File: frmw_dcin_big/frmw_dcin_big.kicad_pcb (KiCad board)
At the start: 2 copper layers, 41.5 x 24 mm, 55 parts, among them J2 SMART, M1 AltmodeFriend, Q1 SI4909, Q2 2N7002, Q3 2N7002, Q4 2N7002, Q5 SI4909, Q6 2N7002, Q7 SI4909, U1 SY6280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

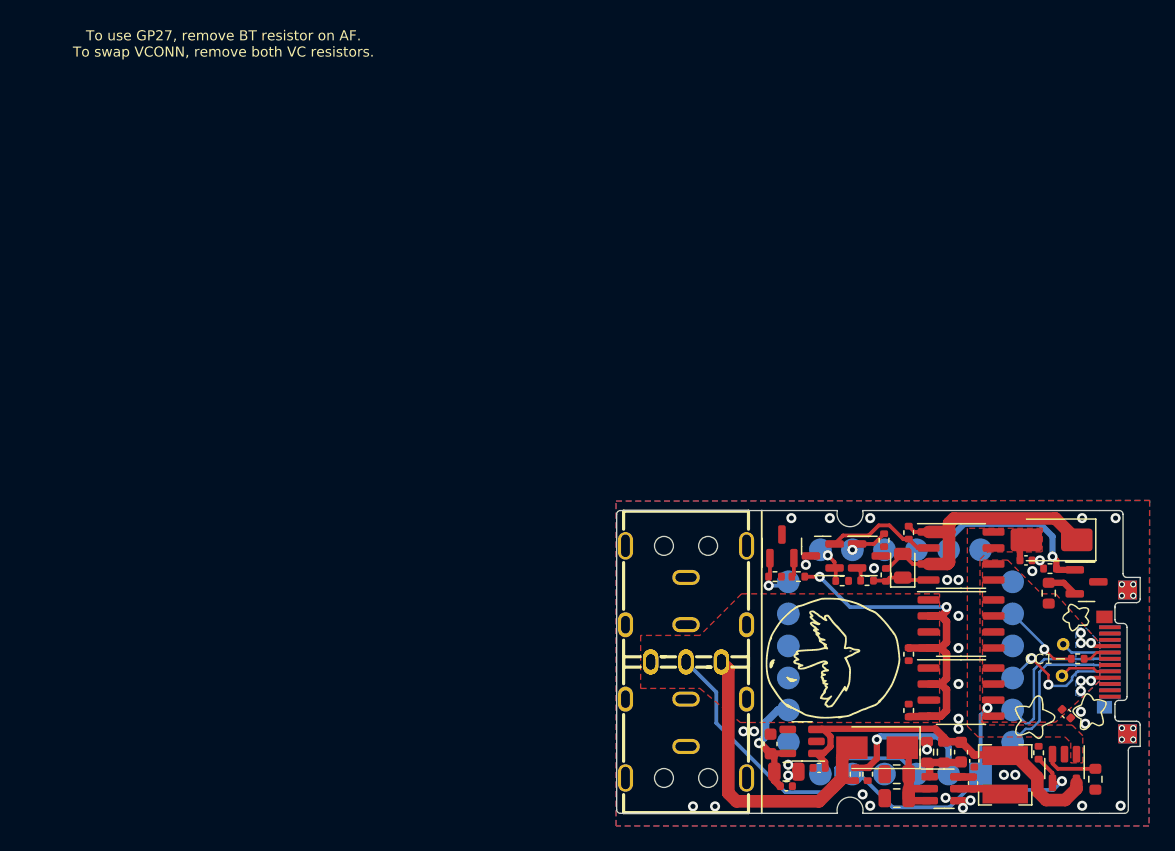
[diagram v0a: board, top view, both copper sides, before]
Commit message: design: reviewed. added a proper circuit for HP/Dell center pin detection, did BOM optimizations, recalculated SY6280 resistors, yote via-in-pad, improved tracks and fills, updated USB-C footprint
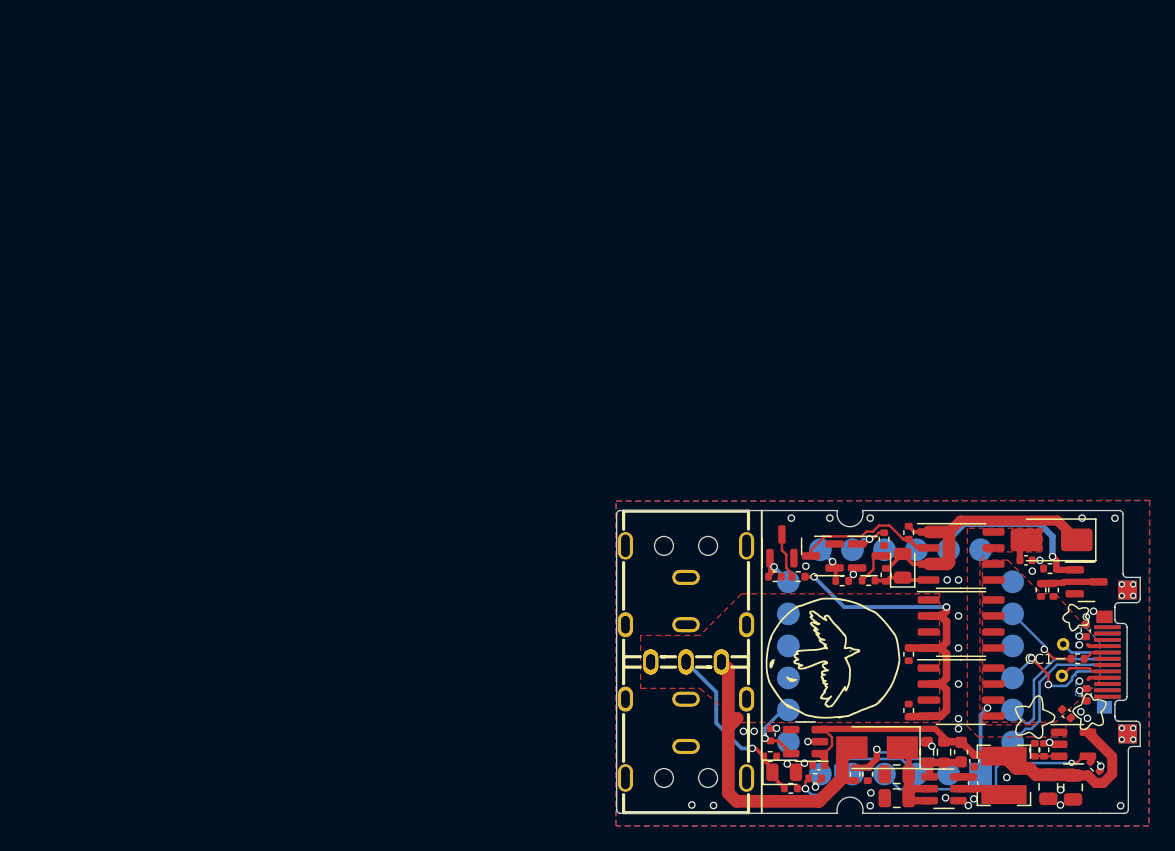
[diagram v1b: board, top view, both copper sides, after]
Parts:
- added C12: 10nF, Capacitor_SMD:C_0402_1005Metric, F.Cu at (137.7, 77.5)
- added C13: 10nF, Capacitor_SMD:C_0402_1005Metric, F.Cu at (137.8, 82.6)
- added C14: 10nF, Capacitor_SMD:C_0402_1005Metric, B.Cu at (137.8, 82.6)
- added C15: 10nF, Capacitor_SMD:C_0402_1005Metric, B.Cu at (137.7, 77.5)
- added D2: 3V6, Diode_SMD:D_0805_2012Metric, F.Cu at (113.8, 88.8)
- added R11: 1K8, Resistor_SMD:R_0402_1005Metric, F.Cu at (134.1, 74.3)
- added R14: 1K8, Resistor_SMD:R_0402_1005Metric, F.Cu at (135.1, 74.3)
- added R2: 20K, Resistor_SMD:R_0402_1005Metric, F.Cu at (112.7, 87.5)
- added R3: 5K1, Resistor_SMD:R_0402_1005Metric, F.Cu at (116.2, 89.2)
- added R5: 0R, Resistor_SMD:R_0402_1005Metric, F.Cu at (114.3, 90.0)
- C4: footprint Capacitor_SMD:C_0603_1608Metric -> Capacitor_SMD:C_0805_2012Metric
- D1: value D_Small -> Schottky 1A
- R1: value 0R -> NC
- R19: value 1K -> 20K; footprint Resistor_SMD:R_0603_1608Metric -> Resistor_SMD:R_0402_1005Metric
- R22: value 1K -> 1K8
- R23: value 10K -> 20K
- R6: renamed from ISET1; value x -> 5K1; footprint Resistor_SMD:R_0603_1608Metric -> Resistor_SMD:R_0402_1005Metric
- moved C3 22.8 mm to (136.7, 90.0), turned to -90 degrees
- moved C4 22.3 mm to (134.7, 89.9), turned to -90 degrees
- moved R19 12.5 mm to (133.7, 87.0)
- moved R6 4.70 mm to (134.4, 87.0), turned to 90 degrees
- moved R21 4.62 mm to (138.4, 88.3), turned to -45 degrees
- moved C7 4.27 mm to (112.7, 85.8), turned to 90 degrees
- moved U1 2.06 mm to (136.7, 86.5), turned to 0 degrees
- moved U3 0.27 mm to (115.5, 86.3)
- moved C9 0.21 mm to (116.5, 88.2)
- moved R18 0.12 mm to (120.5, 73.5)
- moved L1 0.11 mm to (131.2, 89.0)
- moved R13 0.08 mm to (121.7, 70.3)
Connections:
- C3 pad 1: +3.3V -> +5V
- C4 pad 1: +3.3V -> +5V
- M1 pad 3: /HD_PSID -> /PSID_R
- M1 pad 4: unconnected-(M1-GP0-Pad4) -> /SY_EN
- M1 pad 5: /SY_EN -> unconnected-(M1-GP1-Pad5)
- M1 pad 6: unconnected-(M1-GP2-Pad6) -> /PSID_PU_EN
- Q2 pad 2: Net-(Q2-S) -> GND
- Q2 pad 3: GND -> Net-(Q2-D)
- Q3 pad 2: Net-(Q3-S) -> GND
- Q3 pad 3: GND -> Net-(Q3-D)
- Q4 pad 2: Net-(Q4-S) -> GND
- Q4 pad 3: GND -> Net-(Q4-D)
- Q5 pad 2: Net-(Q2-S) -> Net-(Q2-D)
- Q6 pad 2: Net-(Q6-S) -> GND
- Q6 pad 3: GND -> Net-(Q6-D)
- R12 pad 2: Net-(Q2-S) -> Net-(Q2-D)
- R18 pad 2: Net-(Q6-S) -> Net-(Q6-D)
- R19 pad 1: VBUS -> Net-(U1-ISET)
- R19 pad 2: Net-(Q4-S) -> GND
- R8 pad 2: Net-(Q3-S) -> Net-(Q3-D)
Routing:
- net /PSID_R: track 0.00 -> 13.1 mm, vias 0 -> 1
- net /HD_PSID: track 26.4 -> 14.0 mm, vias 0 -> 1
- net Net-(Q2-D): track 0.00 -> 11.3 mm
- net Net-(Q2-S): track 8.80 -> 0.00 mm
- net +5V: track 30.1 -> 35.3 mm
- net Net-(Q4-D): track 0.00 -> 4.96 mm
- net GND: track 0.00 -> 3.73 mm, vias 42 -> 48
- net +3.3V: track 9.60 -> 5.93 mm
- net Net-(Q3-D): track 0.00 -> 3.66 mm
- net Net-(Q6-D): track 0.00 -> 2.76 mm
- net /VIN_ADC: track 11.8 -> 9.26 mm
- net /SY_EN: track 21.7 -> 19.1 mm
- net Net-(Q4-S): track 2.42 -> 0.00 mm
- net Net-(U1-ISET): track 4.31 -> 1.93 mm
- net /PSID_PU_EN: track 0.00 -> 2.09 mm, vias 0 -> 1
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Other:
- board text removed: "To use GP27, remove BT resistor on AF. To swap VCONN, remove both VC resistors."

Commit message: Added name and logo
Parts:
- removed the G*** at (117.5, 79.8)
- G***: moved to B.Cu
- moved G*** 11.6 mm to (125.4, 79.2), turned to 90 degrees
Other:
- board text added: "DC-CC v1 by WifiCable and Arya"
- board text removed: "<NAME TBD> v1 by WifiCable and Arya"
